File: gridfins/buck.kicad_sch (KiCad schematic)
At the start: 30 parts, among them Q1 SSM3K15AMFV,L3F, U6 SiC437AED-T1

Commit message: update 2
Renamed repeated resistor names. Changed typo in buck - removing the 442k resistor actually changes Vout to 7.4V not 8.4! We need 7.4V for servos.
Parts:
- removed R20: 10k, Resistor_SMD:R_0402_1005Metric, symbol Device:R_Small
- removed R21: 2.2, Resistor_SMD:R_0402_1005Metric, symbol Device:R_Small
- added R28: 10k, Resistor_SMD:R_0402_1005Metric, symbol Device:R_Small
- added R29: 2.2, Resistor_SMD:R_0402_1005Metric, symbol Device:R_Small
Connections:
- net PGOOD: now also R28.2
- net PHASE: now also R29.1
- net VDD: now also R28.1
- net at C39.2: now also R29.2
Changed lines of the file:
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@@
 		)
 	)
-	(text_box "Remove this resistor for 8.4V mode"
+	(text_box "Remove this resistor for 7.4V mode"
 		(exclude_from_sim no)
 		(at 138.43 39.37 0)
@@
 		(stroke
 			(width -0.0001)
-			(type default)
+			(type solid)
 		)
 		(fill
@@
 	)
 	(symbol
-		(lib_id "Device:R_Small")
-		(at 67.31 91.44 90)
-		(unit 1)
-		(exclude_from_sim no)
-		(in_bom yes)
-		(on_board yes)
-		(dnp no)
-		(property "Reference" "R20"
-			(at 67.31 93.218 90)
-			(effects
-				(font
-					(size 1.27 1.27)
-				)
-			)
-		)
-		(property "Value" "10k"
-			(at 60.96 92.7069 90)
-			(effects
-				(font
-					(size 1.27 1.27)
-				)
-			)
-		)
-		(property "Footprint" "Resistor_SMD:R_0402_1005Metric"
-			(at 67.31 91.44 0)
-			(effects
-				(font
-					(size 1.27 1.27)
-				)
-				(hide yes)
-			)
-		)
-		(property "Datasheet" "~"
-			(at 67.31 91.44 0)
-			(effects
-				(font
-					(size 1.27 1.27)
-				)
-				(hide yes)
-			)
-		)
-		(property "Description" ""
-			(at 67.31 91.44 0)
-			(effects
-				(font
-					(size 1.27 1.27)
-				)
-				(hide yes)
-			)
-		)
-		(pin "1"
-		)
-		(pin "2"
-		)
-		(instances
-			(project "RicardoTemplate"
-				(path "/7db990e4-92e1-4f99-b4d2-435bbec1ba83/80cb323d-06df-474c-a120-f147460ae20e"
-					(reference "R20")
-					(unit 1)
-				)
-			)
-		)
-	)
-	(symbol
 		(lib_id "power:GND")
 		(at 138.43 127 0)
@@
 	(symbol
 		(lib_id "Device:R_Small")
+		(at 67.31 91.44 90)
+		(unit 1)
+		(exclude_from_sim no)
+		(in_bom yes)
+		(on_board yes)
+		(dnp no)
+		(property "Reference" "R28"
+			(at 67.31 93.218 90)
+			(effects
+				(font
+					(size 1.27 1.27)
+				)
+			)
+		)
+		(property "Value" "10k"
+			(at 60.96 92.7069 90)
+			(effects
+				(font
+					(size 1.27 1.27)
+				)
+			)
+		)
+		(property "Footprint" "Resistor_SMD:R_0402_1005Metric"
+			(at 67.31 91.44 0)
+			(effects
+				(font
+					(size 1.27 1.27)
+				)
+				(hide yes)
+			)
+		)
+		(property "Datasheet" "~"
+			(at 67.31 91.44 0)
+			(effects
+				(font
+					(size 1.27 1.27)
+				)
+				(hide yes)
+			)
+		)
+		(property "Description" ""
+			(at 67.31 91.44 0)
+			(effects
+				(font
+					(size 1.27 1.27)
+				)
+				(hide yes)
+			)
+		)
+		(pin "1"
+		)
+		(pin "2"
+		)
+		(instances
+			(project "gridfins"
+				(path "/7db990e4-92e1-4f99-b4d2-435bbec1ba83/80cb323d-06df-474c-a120-f147460ae20e"
+					(reference "R28")
+					(unit 1)
+				)
+			)
+		)
+	)
+	(symbol
+		(lib_id "Device:R_Small")
 		(at 130.81 54.61 180)
 		(unit 1)
@@
 	)
 	(symbol
+		(lib_id "Device:R_Small")
+		(at 134.62 78.74 90)
+		(unit 1)
+		(exclude_from_sim no)
+		(in_bom yes)
+		(on_board yes)
+		(dnp no)
+		(property "Reference" "R29"
+			(at 134.4945 80.972 90)
+			(effects
+				(font
+					(size 1.27 1.27)
+				)
+			)
+		)
+		(property "Value" "2.2"
+			(at 134.4945 83.5089 90)
+			(effects
+				(font
+					(size 1.27 1.27)
+				)
+			)
+		)
+		(property "Footprint" "Resistor_SMD:R_0402_1005Metric"
+			(at 134.62 78.74 0)
+			(effects
+				(font
+					(size 1.27 1.27)
+				)
+				(hide yes)
+			)
+		)
+		(property "Datasheet" "~"
+			(at 134.62 78.74 0)
+			(effects
+				(font
+					(size 1.27 1.27)
+				)
+				(hide yes)
+			)
+		)
+		(property "Description" ""
+			(at 134.62 78.74 0)
+			(effects
+				(font
+					(size 1.27 1.27)
+				)
+				(hide yes)
+			)
+		)
+		(pin "1"
+		)
+		(pin "2"
+		)
+		(instances
+			(project "gridfins"
+				(path "/7db990e4-92e1-4f99-b4d2-435bbec1ba83/80cb323d-06df-474c-a120-f147460ae20e"
+					(reference "R29")
+					(unit 1)
+				)
+			)
+		)
+	)
+	(symbol
 		(lib_id "Device:C_Small")
 		(at 222.25 67.31 0)
@@
 					(unit 1)
 				)
-			)
-		)
-	)
-	(symbol
-		(lib_id "Device:R_Small")
-		(at 134.62 78.74 90)
-		(unit 1)
-		(exclude_from_sim no)
-		(in_bom yes)
-		(on_board yes)
-		(dnp no)
-		(property "Reference" "R21"
-			(at 134.4945 80.972 90)
-			(effects
-				(font
-					(size 1.27 1.27)
-				)
-			)
-		)
-		(property "Value" "2.2"
-			(at 134.4945 83.5089 90)
-			(effects
-				(font
-					(size 1.27 1.27)
-				)
-			)
-		)
-		(property "Footprint" "Resistor_SMD:R_0402_1005Metric"
-			(at 134.62 78.74 0)
-			(effects
-				(font
-					(size 1.27 1.27)
-				)
-				(hide yes)
-			)
-		)
-		(property "Datasheet" "~"
-			(at 134.62 78.74 0)
-			(effects
-				(font
-					(size 1.27 1.27)
-				)
-				(hide yes)
-			)
-		)
-		(property "Description" ""
-			(at 134.62 78.74 0)
-			(effects
-				(font
-					(size 1.27 1.27)
-				)
-				(hide yes)
-			)
-		)
-		(pin "1"
-		)
-		(pin "2"
-		)
-		(instances
-			(project "RicardoTemplate"
-				(path "/7db990e4-92e1-4f99-b4d2-435bbec1ba83/80cb323d-06df-474c-a120-f147460ae20e"
-					(reference "R21")
-					(unit 1)
-				)

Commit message: update 3
added tvs diode chip module for 3rd servo
added net connection to actuators sheet
changed 6 to 7.4 label
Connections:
- net +6V renamed +7.4V
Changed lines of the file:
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@@
 			)
 		)
-		(property "Value" "+6V"
+		(property "Value" "+7.4V"
 			(at 226.8053 62.8978 0)
 			(effects
@@
 			)
 		)
-		(property "Value" "+6V"
+		(property "Value" "+7.4V"
 			(at 112.5053 121.3178 0)
 			(effects

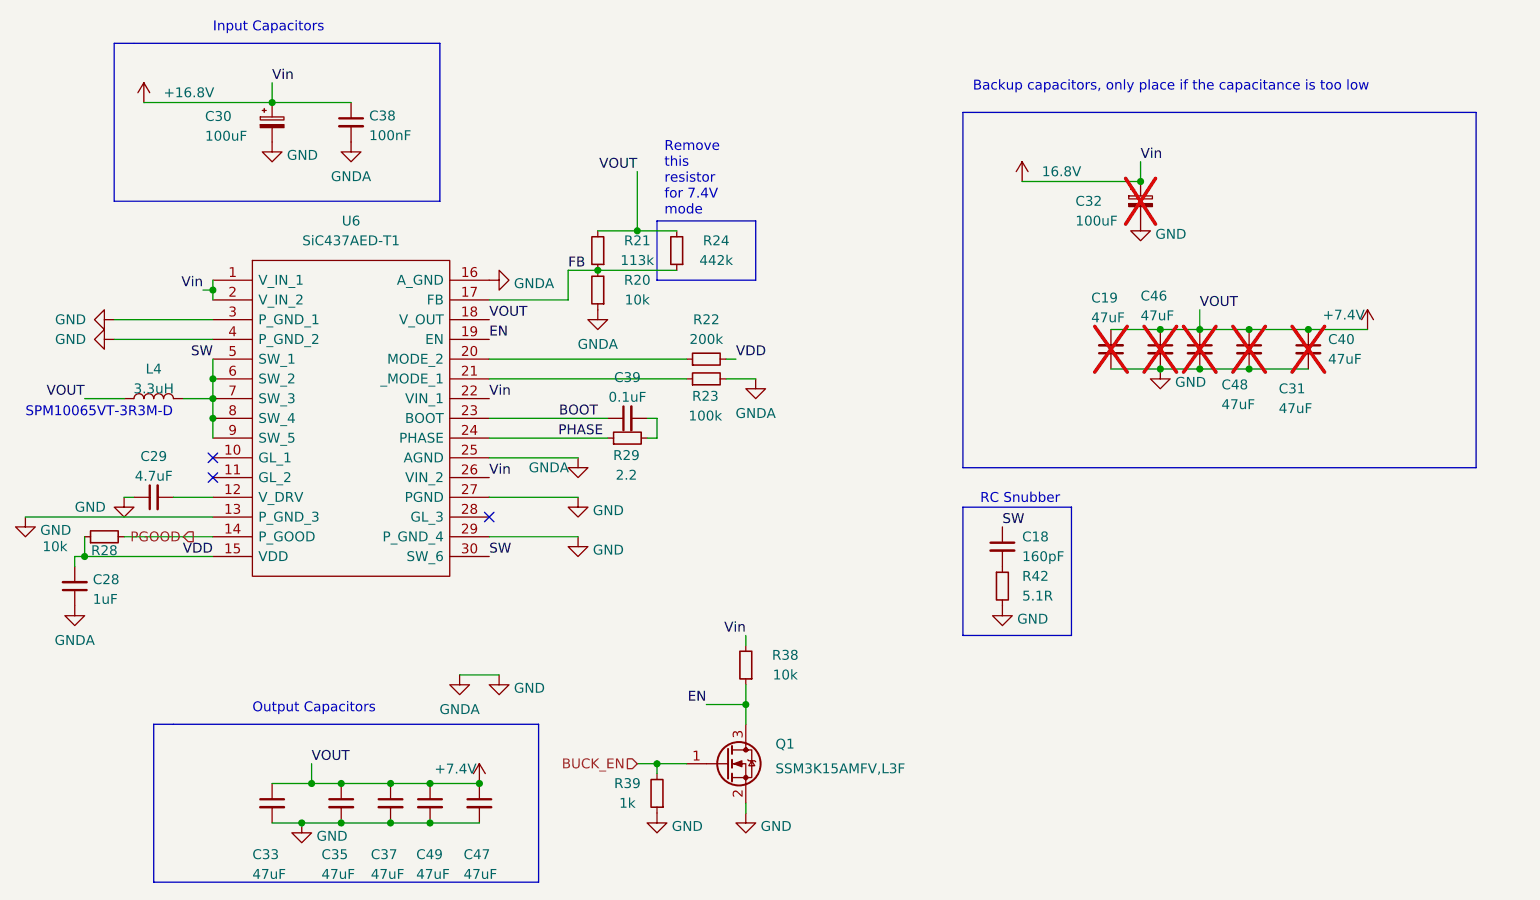
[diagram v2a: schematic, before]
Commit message: Deployment Power Cut Mechanism
Employed the master high-side switch from flintandsteel to disable servo and linear actuator power once lower altitude limit reached. This will prevent electrical problems during touchdown:

Routed power rail 16.8V to switch input. Switch output routed to buck input. When high-side switch is enabled, buck input voltage is pulled down, depowering the servos and linear actuator.
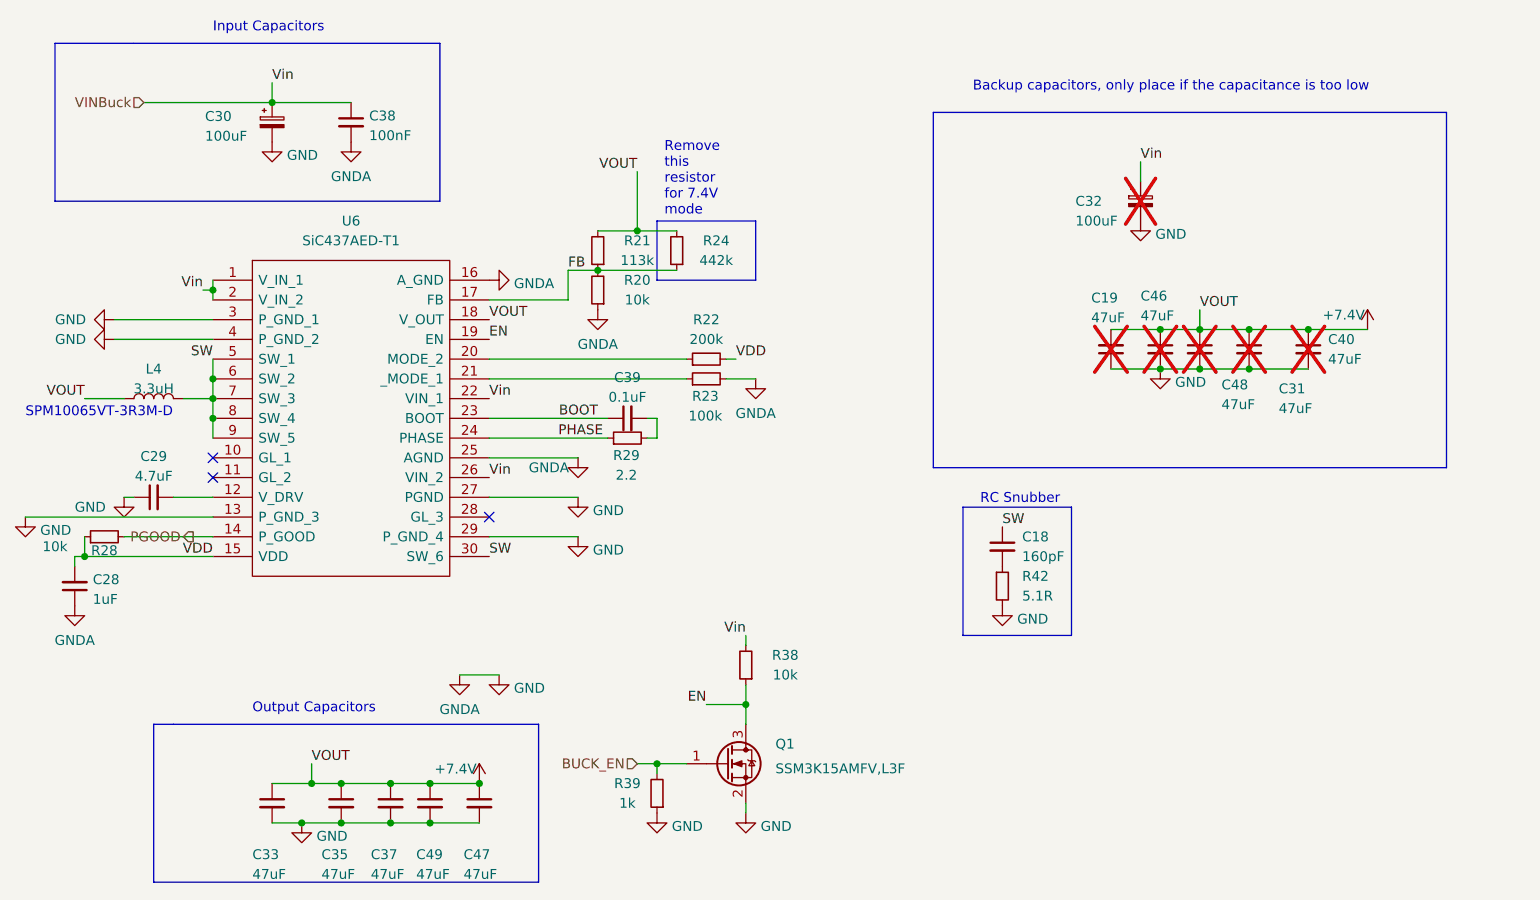
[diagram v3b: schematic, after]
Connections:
- net +16.8V renamed VINBuck
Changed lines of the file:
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@@
 	(paper "A4")
 	(rectangle
-		(start 177.8 36.83)
-		(end 243.84 82.55)
+		(start 173.99 36.83)
+		(end 240.03 82.55)
 		(stroke
 			(width 0)
@@
 	)
 	(junction
-		(at 200.66 45.72)
-		(diameter 0)
-		(color 0 0 0 0)
-	)
-	(junction
 		(at 135.89 52.07)
 		(diameter 0)
@@
 	(polyline
 		(pts
-			(xy 68.58 27.94) (xy 71.12 27.94)
+			(xy 60.96 27.94) (xy 71.12 27.94)
 		)
 		(stroke
@@
 	(polyline
 		(pts
-			(xy 110.49 48.26) (xy 68.58 48.26)
+			(xy 110.49 48.26) (xy 60.96 48.26)
 		)
 		(stroke
@@
 	(polyline
 		(pts
-			(xy 68.58 48.26) (xy 68.58 27.94)
+			(xy 60.96 48.26) (xy 60.96 27.94)
 		)
 		(stroke
@@
 		(pts
 			(xy 128.27 86.36) (xy 116.84 86.36)
-		)
-		(stroke
-			(width 0)
-			(type default)
-		)
-	)
-	(wire
-		(pts
-			(xy 185.42 45.72) (xy 200.66 45.72)
 		)
 		(stroke
@@
 			)
 			(justify right bottom)
+		)
+	)
+	(hierarchical_label "VINBuck"
+		(shape input)
+		(at 72.39 35.56 180)
+		(effects
+			(font
+				(size 1.27 1.27)
+			)
+			(justify right)
 		)
 	)
@@
 	)
 	(symbol
-		(lib_id "power:+12V")
-		(at 185.42 45.72 0)
-		(unit 1)
-		(exclude_from_sim no)
-		(in_bom yes)
-		(on_board yes)
-		(dnp no)
-		(fields_autoplaced yes)
-		(property "Reference" "#PWR075"
-			(at 185.42 49.53 0)
-			(effects
-				(font
-					(size 1.27 1.27)
-				)
-				(hide yes)
-			)
-		)
-		(property "Value" "16.8V"
-			(at 187.96 44.4499 0)
-			(effects
-				(font
-					(size 1.27 1.27)
-				)
-				(justify left)
-			)
-		)
-		(property "Footprint" ""
-			(at 185.42 45.72 0)
-			(effects
-				(font
-					(size 1.27 1.27)
-				)
-				(hide yes)
-			)
-		)
-		(property "Datasheet" ""
-			(at 185.42 45.72 0)
-			(effects
-				(font
-					(size 1.27 1.27)
-				)
-				(hide yes)
-			)
-		)
-		(property "Description" ""
-			(at 185.42 45.72 0)
-			(effects
-				(font
-					(size 1.27 1.27)
-				)
-				(hide yes)
-			)
-		)
-		(pin "1"
-		)
-		(instances
-			(project "RicardoTemplate"
-				(path "/7db990e4-92e1-4f99-b4d2-435bbec1ba83/80cb323d-06df-474c-a120-f147460ae20e"
-					(reference "#PWR075")
-					(unit 1)
-				)
-			)
-		)
-	)
-	(symbol
 		(lib_id "power:GNDA")
 		(at 130.81 62.23 0)
@@
 					(unit 1)
 				)
-			)
-		)
-	)
-	(symbol
-		(lib_id "power:+12V")
-		(at 72.39 35.56 0)
-		(unit 1)
-		(exclude_from_sim no)
-		(in_bom yes)
-		(on_board yes)
-		(dnp no)
-		(fields_autoplaced yes)
-		(property "Reference" "#PWR062"
-			(at 72.39 39.37 0)
-			(effects
-				(font
-					(size 1.27 1.27)
-				)
-				(hide yes)
-			)
-		)
-		(property "Value" "+16.8V"
-			(at 74.93 34.2899 0)
-			(effects
-				(font
-					(size 1.27 1.27)
-				)
-				(justify left)
-			)
-		)
-		(property "Footprint" ""
-			(at 72.39 35.56 0)
-			(effects
-				(font
-					(size 1.27 1.27)
-				)
-				(hide yes)
-			)
-		)
-		(property "Datasheet" ""
-			(at 72.39 35.56 0)
-			(effects
-				(font
-					(size 1.27 1.27)
-				)
-				(hide yes)
-			)
-		)
-		(property "Description" ""
-			(at 72.39 35.56 0)
-			(effects
-				(font
-					(size 1.27 1.27)
-				)
-				(hide yes)
-			)
-		)
-		(pin "1"
-		)
-		(instances
-			(project "RicardoTemplate"
-				(path "/7db990e4-92e1-4f99-b4d2-435bbec1ba83/80cb323d-06df-474c-a120-f147460ae20e"
-					(reference "#PWR062")
-					(unit 1)
-				)
